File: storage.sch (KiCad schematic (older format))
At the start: 1 part

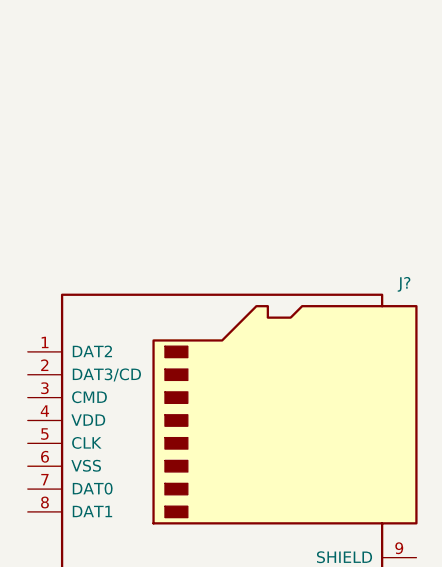
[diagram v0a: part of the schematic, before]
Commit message: Added some footprints. Basic board outline.
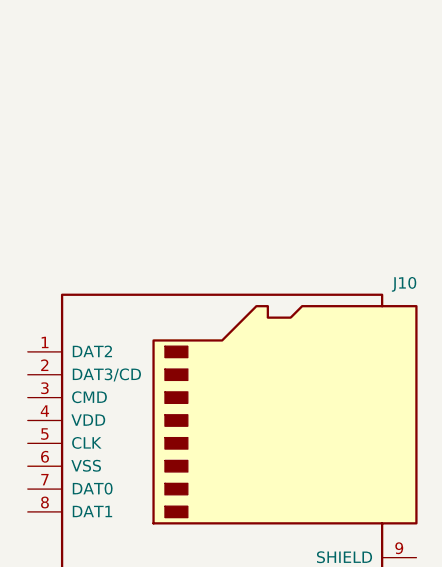
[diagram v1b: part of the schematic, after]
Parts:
- J10: renamed from J?; footprint (none) -> Amphenol SD Card:1140084168
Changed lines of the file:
@@
 $Descr A4 11693 8268
 encoding utf-8
-Sheet 8 11
+Sheet 6 11
 Title "Neotron 32K"
 Date "2019-12-08"
@@
 P 5550 3300
 AR Path="/5DF3DCD4" Ref="J?"  Part="1"
-AR Path="/5DF1D0B0/5DF3DCD4" Ref="J?"  Part="1"
-F 0 "J?" H 6300 3900 50  0000 C CNN
+AR Path="/5DF1D0B0/5DF3DCD4" Ref="J10"  Part="1"
+F 0 "J10" H 6300 3900 50  0000 C CNN
 F 1 "Amphenol 114-00841-68" H 5550 2600 50  0000 C CNN
-F 2 "" H 5550 3300 50  0001 C CNN
+F 2 "Amphenol SD Card:1140084168" H 5550 3300 50  0001 C CNN
 F 3 "https://media.digikey.com/pdf/Data%20Sheets/Amphenol%20PDFs/114-00841-68.pdf" H 5550 3300 50  0001 C CNN
 F 4 "114-00841-68-1-ND" H 5550 3300 50  0001 C CNN "Digikey"

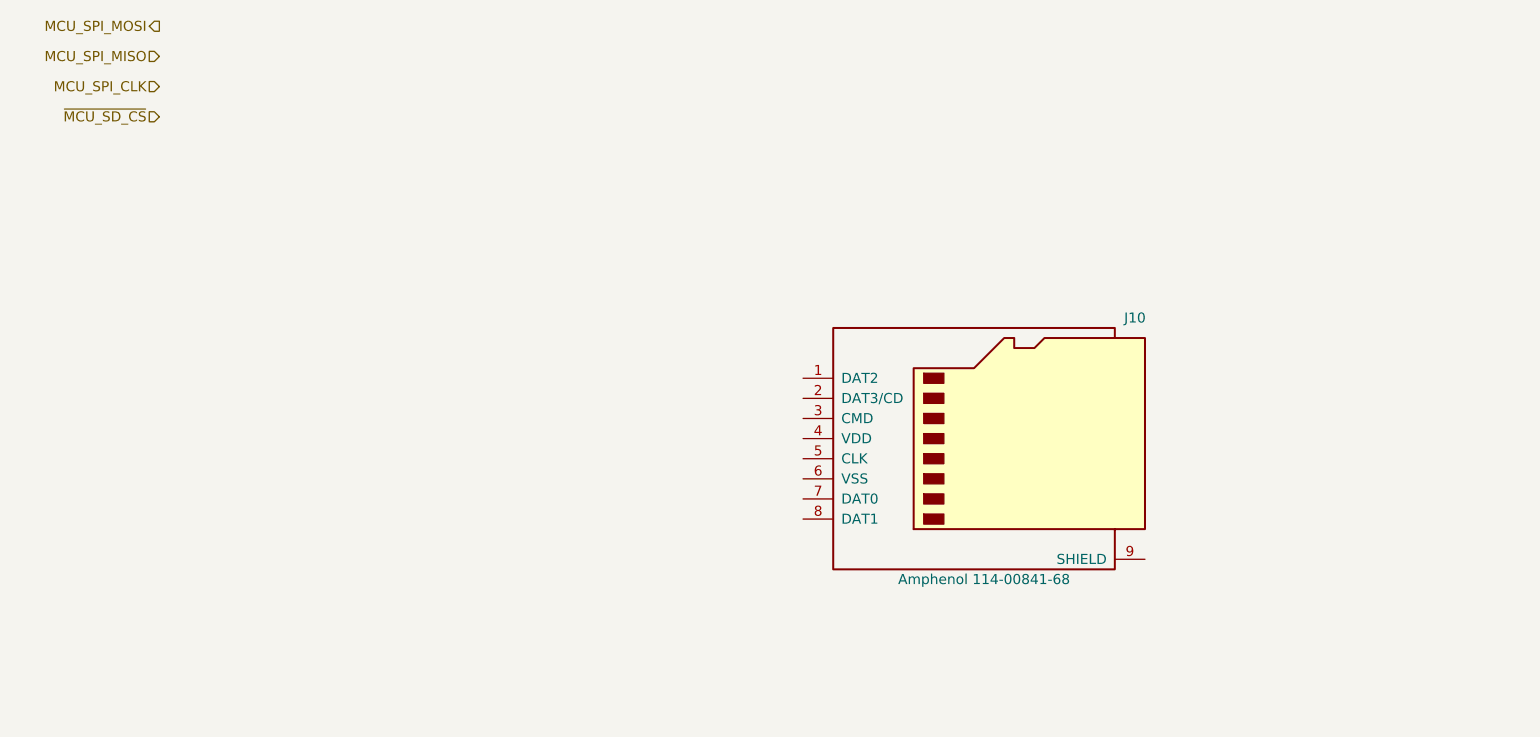
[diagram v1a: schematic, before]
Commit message: Completed Power, SD, MIDI, Parallel and Joystick sheets.
Switch to sheet based 100x part numbering.
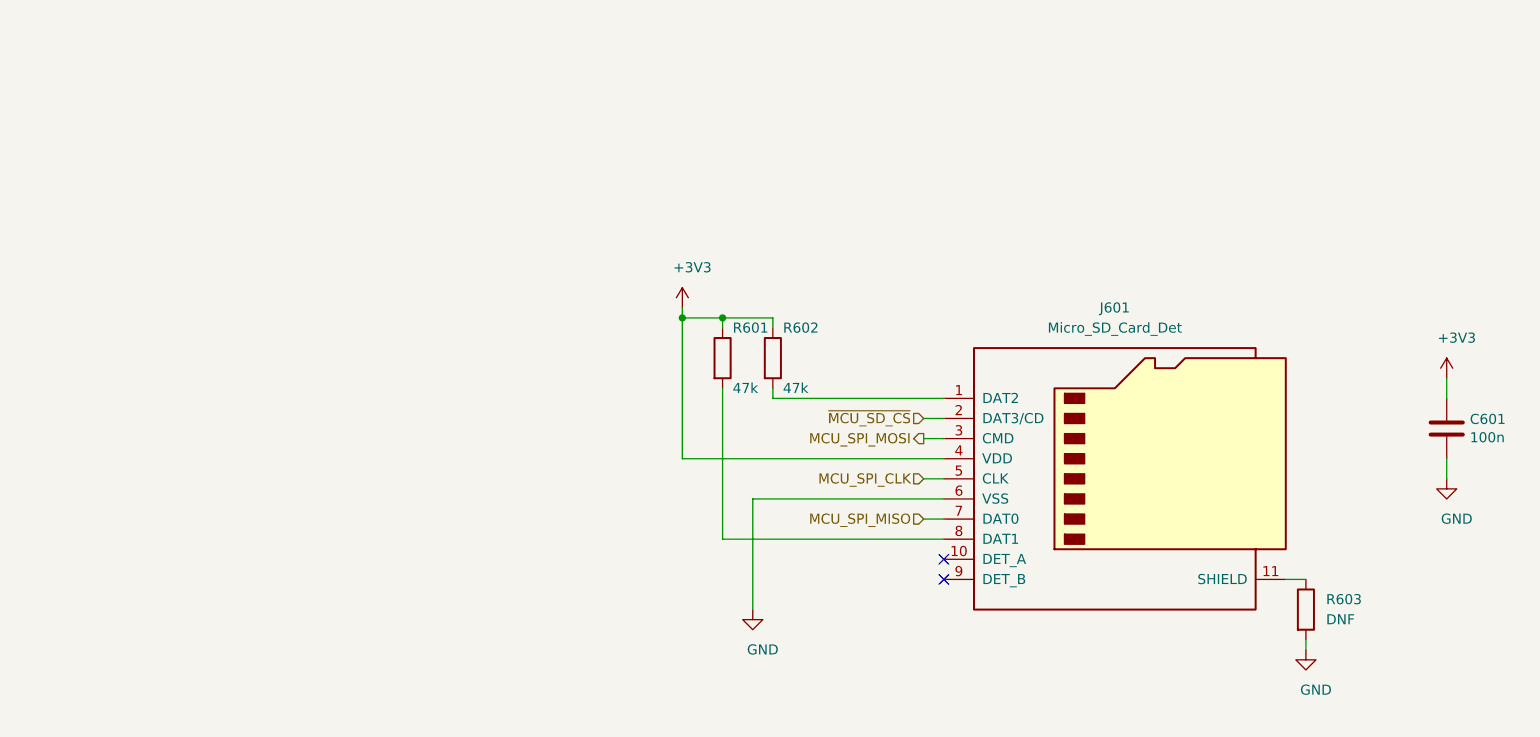
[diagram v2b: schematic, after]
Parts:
- removed J10: Amphenol 114-00841-68, Amphenol SD Card:1140084168, symbol Connector:Micro_SD_Card
- added C601: 100n, Capacitor_THT:C_Disc_D3.0mm_W2.0mm_P2.50mm, symbol Device:C
- added J601: Micro_SD_Card_Det, symbol Connector:Micro_SD_Card_Det
- added R601, R602: 47k, symbol Device:R
- added R603: DNF, symbol Device:R
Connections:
- net MCU_SPI_CLK: now also J601.5 (CLK)
- net MCU_SPI_MISO: now also J601.7 (DAT0)
- net MCU_SPI_MOSI: now also J601.3 (CMD)
- net ~MCU_SD_CS: now also J601.2 (DAT3/CD)
- new net: J601.1 (DAT2), R602.2
- new net: J601.11 (SHIELD), R603.1
- new net: J601.8 (DAT1), R601.2
- new net +3V3: C601.1, J601.4 (VDD), R601.1, R602.1
- new net GND: C601.2, J601.6 (VSS), R603.2
- no-connect marks 0 -> 2
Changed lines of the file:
@@
 Comment4 ""
 $EndDescr
+Text HLabel 5250 3300 0    50   Output ~ 0
+MCU_SPI_MOSI
+Text HLabel 5250 3700 0    50   Input ~ 0
+MCU_SPI_MISO
+Text HLabel 5250 3500 0    50   Input ~ 0
+MCU_SPI_CLK
+Text HLabel 5250 3200 0    50   Input ~ 0
+~MCU_SD_CS
 $Comp
-L Connector:Micro_SD_Card J?
-U 1 1 5DF3DCD4
-P 5550 3300
-AR Path="/5DF3DCD4" Ref="J?"  Part="1"
-AR Path="/5DF1D0B0/5DF3DCD4" Ref="J10"  Part="1"
-F 0 "J10" H 6300 3900 50  0000 C CNN
-F 1 "Amphenol 114-00841-68" H 5550 2600 50  0000 C CNN
-F 2 "Amphenol SD Card:1140084168" H 5550 3300 50  0001 C CNN
-F 3 "https://media.digikey.com/pdf/Data%20Sheets/Amphenol%20PDFs/114-00841-68.pdf" H 5550 3300 50  0001 C CNN
-F 4 "114-00841-68-1-ND" H 5550 3300 50  0001 C CNN "Digikey"
-	1    5550 3300
+L Connector:Micro_SD_Card_Det J601
+U 1 1 5DF22812
+P 6250 3500
+F 0 "J601" H 6200 4350 50  0000 C CNN
+F 1 "Micro_SD_Card_Det" H 6200 4250 50  0000 C CNN
+F 2 "" H 8300 4200 50  0001 C CNN
+F 3 "https://www.hirose.com/product/en/download_file/key_name/DM3/category/Catalog/doc_file_id/49662/?file_category_id=4&item_id=195&is_series=1" H 6250 3600 50  0001 C CNN
+	1    6250 3500
 	1    0    0    -1
 $EndComp
-Text HLabel 1450 1250 0    50   Output ~ 0
-MCU_SPI_MOSI
-Text HLabel 1450 1400 0    50   Input ~ 0
-MCU_SPI_MISO
-Text HLabel 1450 1550 0    50   Input ~ 0
-MCU_SPI_CLK
-Text HLabel 1450 1700 0    50   Input ~ 0
-~MCU_SD_CS
+$Comp
+L power:+3V3 #PWR0601
+U 1 1 5DF24158
+P 4050 2650
+F 0 "#PWR0601" H 4050 2500 50  0001 C CNN
+F 1 "+3V3" H 4100 2850 50  0000 C CNN
+F 2 "" H 4050 2650 50  0001 C CNN
+F 3 "" H 4050 2650 50  0001 C CNN
+	1    4050 2650
+	1    0    0    -1
+$EndComp
+$Comp
+L power:GND #PWR0602
+U 1 1 5DF24591
+P 4400 4150
+F 0 "#PWR0602" H 4400 3900 50  0001 C CNN
+F 1 "GND" H 4450 3950 50  0000 C CNN
+F 2 "" H 4400 4150 50  0001 C CNN
+F 3 "" H 4400 4150 50  0001 C CNN
+	1    4400 4150
+	1    0    0    -1
+$EndComp
+Wire Wire Line
+	4400 3600 5350 3600
+$Comp
+L power:GND #PWR0603
+U 1 1 5DF25504
+P 7150 4350
+F 0 "#PWR0603" H 7150 4100 50  0001 C CNN
+F 1 "GND" H 7200 4150 50  0000 C CNN
+F 2 "" H 7150 4350 50  0001 C CNN
+F 3 "" H 7150 4350 50  0001 C CNN
+	1    7150 4350
+	1    0    0    -1
+$EndComp
+$Comp
+L Device:R R603
+U 1 1 5DF25D3A
+P 7150 4150
+F 0 "R603" H 7250 4200 50  0000 L CNN
+F 1 "DNF" H 7250 4100 50  0000 L CNN
+F 2 "" V 7080 4150 50  0001 C CNN
+F 3 "~" H 7150 4150 50  0001 C CNN
+	1    7150 4150
+	1    0    0    -1
+$EndComp
+Wire Wire Line
+	7050 4000 7150 4000
+Wire Wire Line
+	7150 4300 7150 4350
+Wire Wire Line
+	5250 3200 5350 3200
+Wire Wire Line
+	5250 3300 5350 3300
+Wire Wire Line
+	5250 3500 5350 3500
+Wire Wire Line
+	5250 3700 5350 3700
+$Comp
+L Device:R R601
+U 1 1 5DF267A9
+P 4250 2900
+F 0 "R601" H 4300 3050 50  0000 L CNN
+F 1 "47k" H 4300 2750 50  0000 L CNN
+F 2 "" V 4180 2900 50  0001 C CNN
+F 3 "~" H 4250 2900 50  0001 C CNN
+	1    4250 2900
+	1    0    0    -1
+$EndComp
+$Comp
+L Device:R R602
+U 1 1 5DF273D3
+P 4500 2900
+F 0 "R602" H 4550 3050 50  0000 L CNN
+F 1 "47k" H 4550 2750 50  0000 L CNN
+F 2 "" V 4430 2900 50  0001 C CNN
+F 3 "~" H 4500 2900 50  0001 C CNN
+	1    4500 2900
+	1    0    0    -1
+$EndComp
+Wire Wire Line
+	5350 3100 4500 3100
+Wire Wire Line
+	4500 3100 4500 3050
+Wire Wire Line
+	4250 3800 4250 3050
+Wire Wire Line
+	4050 3400 4050 2700
+Wire Wire Line
+	4050 3400 5350 3400
+Wire Wire Line
+	4400 3600 4400 4150
+Wire Wire Line
+	4050 2700 4250 2700
+Wire Wire Line
+	4250 2700 4250 2750
+Connection ~ 4050 2700
+Wire Wire Line
+	4250 2700 4500 2700
+Wire Wire Line
+	4500 2700 4500 2750
+Connection ~ 4250 2700
+Wire Wire Line
+	4050 2650 4050 2700
+Wire Wire Line
+	4250 3800 5350 3800
+NoConn ~ 5350 3900
+NoConn ~ 5350 4000
+$Comp
+L power:+3V3 #PWR0604
+U 1 1 5E016A44
+P 7850 3000
+F 0 "#PWR0604" H 7850 2850 50  0001 C CNN
+F 1 "+3V3" H 7900 3200 50  0000 C CNN
+F 2 "" H 7850 3000 50  0001 C CNN
+F 3 "" H 7850 3000 50  0001 C CNN
+	1    7850 3000
+	1    0    0    -1
+$EndComp
+$Comp
+L Device:C C601
+U 1 1 5E016EE2
+P 7850 3250
+F 0 "C601" H 7965 3296 50  0000 L CNN
+F 1 "100n" H 7965 3205 50  0000 L CNN
+F 2 "Capacitor_THT:C_Disc_D3.0mm_W2.0mm_P2.50mm" H 7888 3100 50  0001 C CNN
+F 3 "~" H 7850 3250 50  0001 C CNN
+	1    7850 3250
+	1    0    0    -1
+$EndComp
+$Comp
+L power:GND #PWR0605
+U 1 1 5E0170E6
+P 7850 3500
+F 0 "#PWR0605" H 7850 3250 50  0001 C CNN
+F 1 "GND" H 7900 3300 50  0000 C CNN
+F 2 "" H 7850 3500 50  0001 C CNN
+F 3 "" H 7850 3500 50  0001 C CNN
+	1    7850 3500
+	1    0    0    -1
+$EndComp
+Wire Wire Line
+	7850 3000 7850 3100
+Wire Wire Line
+	7850 3400 7850 3500
 $EndSCHEMATC

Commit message: Schematic capture draft complete.
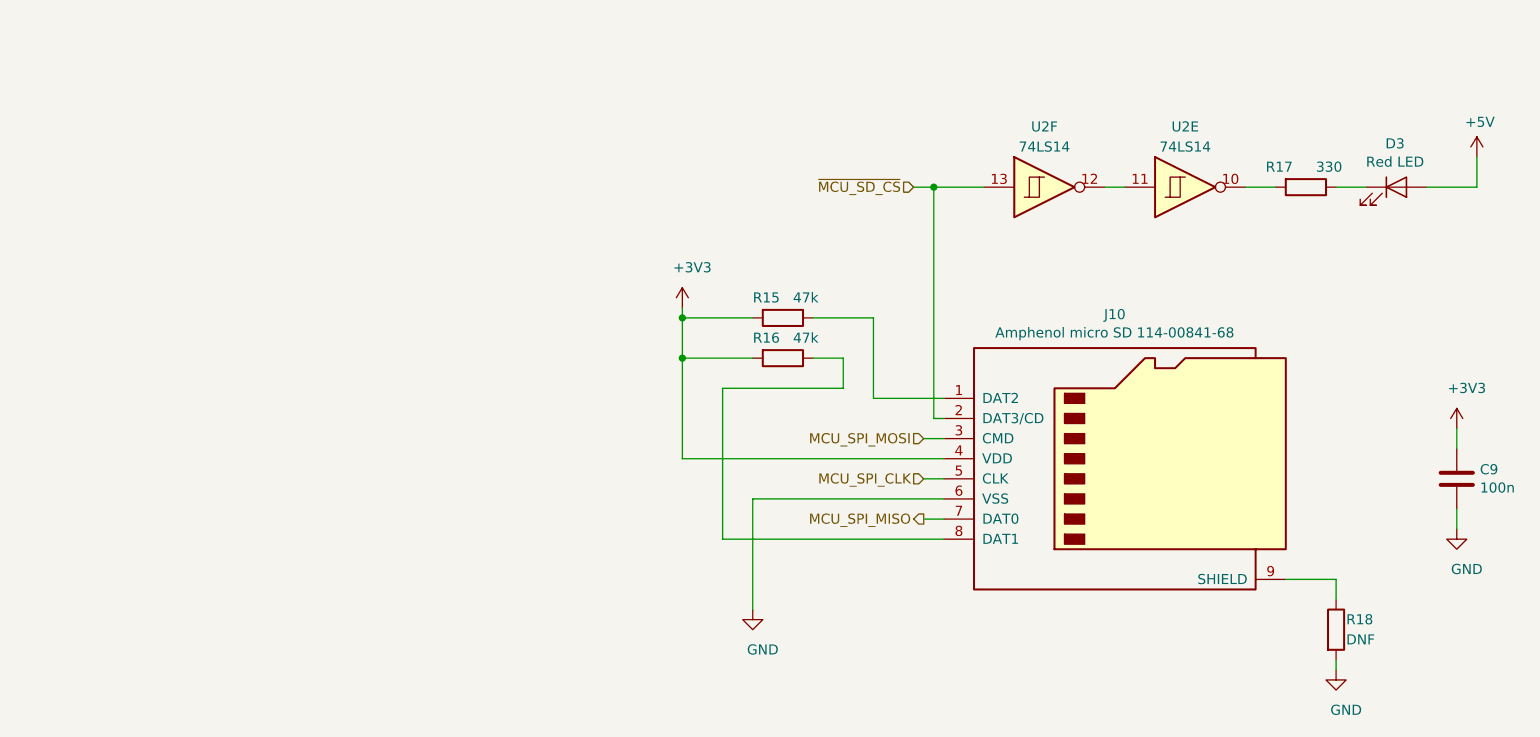
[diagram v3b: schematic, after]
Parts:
- removed J601: Micro_SD_Card_Det, symbol Connector:Micro_SD_Card_Det
- added D3: Red LED, LED_THT:LED_D3.0mm, symbol Device:LED
- added J10: Amphenol micro SD 114-00841-68, Amphenol SD Card:1140084168, symbol Connector:Micro_SD_Card
- added R17: 330, Resistor_THT:R_Axial_DIN0411_L9.9mm_D3.6mm_P12.70mm_Horizontal, symbol Device:R
- added U2: 74LS14, Package_DIP:DIP-14_W7.62mm, symbol 74xx:74LS14
- R15: renamed from R602; footprint (none) -> Resistor_THT:R_Axial_DIN0411_L9.9mm_D3.6mm_P12.70mm_Horizontal
- R16: renamed from R601; footprint (none) -> Resistor_THT:R_Axial_DIN0411_L9.9mm_D3.6mm_P12.70mm_Horizontal
- R18: renamed from R603; footprint (none) -> Resistor_THT:R_Axial_DIN0411_L9.9mm_D3.6mm_P12.70mm_Horizontal
- renumbered C601 to C9
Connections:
- net +3V3: now also R15.2, R16.2, J10.4 (VDD); no longer R15.1, R16.1
- net GND: now also J10.6 (VSS)
- net MCU_SPI_CLK: now also J10.5 (CLK)
- net MCU_SPI_MISO: now also J10.7 (DAT0)
- net MCU_SPI_MOSI: now also J10.3 (CMD)
- net ~MCU_SD_CS: now also J10.2 (DAT3/CD), U2.13
- net at R18.1: now also J10.9 (SHIELD)
- new net: J10.8 (DAT1), R16.1
- new net: J10.1 (DAT2), R15.1
- new net: D3.1 (K), R17.1
- new net: R17.2, U2.10
- new net: U2.11, U2.12
- new net +5V: D3.2 (A)
- no-connect marks 2 -> 0
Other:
- moved on the sheet: C9, R15, R16, R18

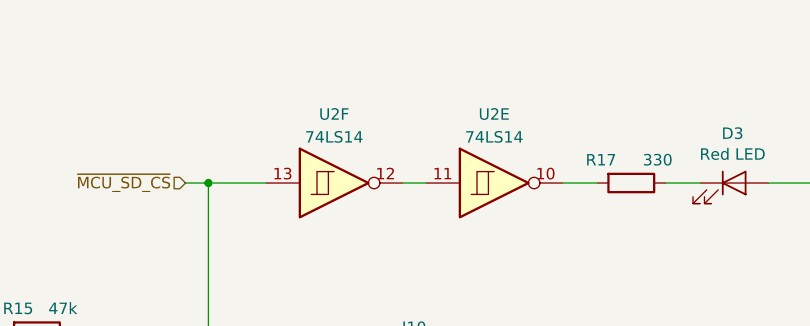
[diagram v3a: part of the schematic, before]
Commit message: Tidied up Atmega power. Added page titles.
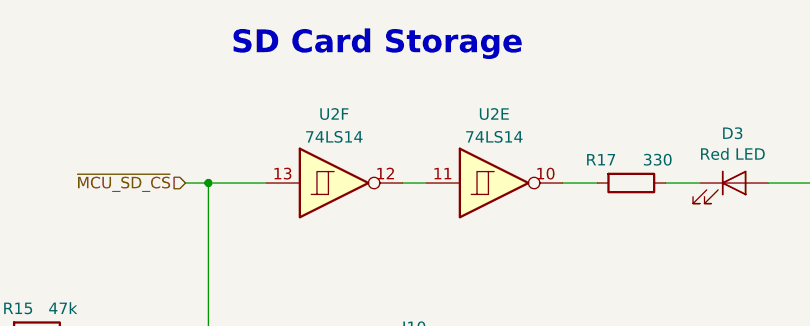
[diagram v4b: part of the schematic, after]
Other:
- note added: "SD Card Storage"
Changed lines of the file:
@@
 Sheet 5 10
 Title "Neotron 32K Main PCB"
-Date "2019-12-15"
-Rev "0.5"
+Date "2019-12-16"
+Rev "0.6"
 Comp "github.com/neotron-compute/Neotron-32-Hardware"
 Comment1 "Copyright (c) Jonathan 'theJPster' Pallant"
@@
 Wire Wire Line
 	4050 2900 4050 3400
+Text Notes 5400 1500 0    100  ~ 20
+SD Card Storage
 $EndSCHEMATC

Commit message: Updated footprints: ) Swapped RS-232 DE9 for IDC header. ) Large caps are radial electrolytics. ) Made resistors a little smaller.
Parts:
- R15, R16, R17, R18: footprint Resistor_THT:R_Axial_DIN0411_L9.9mm_D3.6mm_P12.70mm_Horizontal -> Resistor_THT:R_Axial_DIN0207_L6.3mm_D2.5mm_P10.16mm_Horizontal
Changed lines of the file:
@@
 F 0 "R18" H 7350 4300 50  0000 L CNN
 F 1 "DNF" H 7350 4200 50  0000 L CNN
-F 2 "Resistor_THT:R_Axial_DIN0411_L9.9mm_D3.6mm_P12.70mm_Horizontal" V 7230 4250 50  0001 C CNN
+F 2 "Resistor_THT:R_Axial_DIN0207_L6.3mm_D2.5mm_P10.16mm_Horizontal" V 7230 4250 50  0001 C CNN
 F 3 "~" H 7300 4250 50  0001 C CNN
 	1    7300 4250
@@
 F 0 "R16" V 4450 2750 50  0000 L CNN
 F 1 "47k" V 4450 2950 50  0000 L CNN
-F 2 "Resistor_THT:R_Axial_DIN0411_L9.9mm_D3.6mm_P12.70mm_Horizontal" V 4480 2900 50  0001 C CNN
+F 2 "Resistor_THT:R_Axial_DIN0207_L6.3mm_D2.5mm_P10.16mm_Horizontal" V 4480 2900 50  0001 C CNN
 F 3 "~" H 4550 2900 50  0001 C CNN
 	1    4550 2900
@@
 F 0 "R15" V 4450 2550 50  0000 L CNN
 F 1 "47k" V 4450 2750 50  0000 L CNN
-F 2 "Resistor_THT:R_Axial_DIN0411_L9.9mm_D3.6mm_P12.70mm_Horizontal" V 4480 2700 50  0001 C CNN
+F 2 "Resistor_THT:R_Axial_DIN0207_L6.3mm_D2.5mm_P10.16mm_Horizontal" V 4480 2700 50  0001 C CNN
 F 3 "~" H 4550 2700 50  0001 C CNN
 	1    4550 2700
@@
 F 0 "R17" V 7050 1850 50  0000 L CNN
 F 1 "330" V 7050 2100 50  0000 L CNN
-F 2 "Resistor_THT:R_Axial_DIN0411_L9.9mm_D3.6mm_P12.70mm_Horizontal" V 7080 2050 50  0001 C CNN
+F 2 "Resistor_THT:R_Axial_DIN0207_L6.3mm_D2.5mm_P10.16mm_Horizontal" V 7080 2050 50  0001 C CNN
 F 3 "~" H 7150 2050 50  0001 C CNN
 	1    7150 2050
